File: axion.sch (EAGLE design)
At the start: 148 parts, among them IC1 3.3V, IC2 5V, Q2 12.288Mhz, U10 MIC2039, U11 WM8731, U2 Intel Edison, U4 FT232RLSSOP, U5 PCA9306D, U6 74HC4050, U7 TPA2005D1DGN, X1 MKDSN1,5/2-5,08, X2 ZX62R-AB-5P, X3 ST-005-G, X4 ZX62R-B-5P

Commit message: Change all resistors' package to R0603 (1608)
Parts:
- R1, R10, R11, R12, R13, R14, R15, R16, R17, R18, R19, R2, R20, R21, R22, R23, R24, R3, R30, R31, R32, R34, R36, R37, R4, R5, R6, R7, R8, R9: device resistor:R-US_M1206 -> resistor:R-US_R0603
- R25: device resistor:R-US_0309/V -> resistor:R-US_R0603
- R27, R35, R40, R41, R42, R43, R44: device resistor:R-US_R1206 -> resistor:R-US_R0603

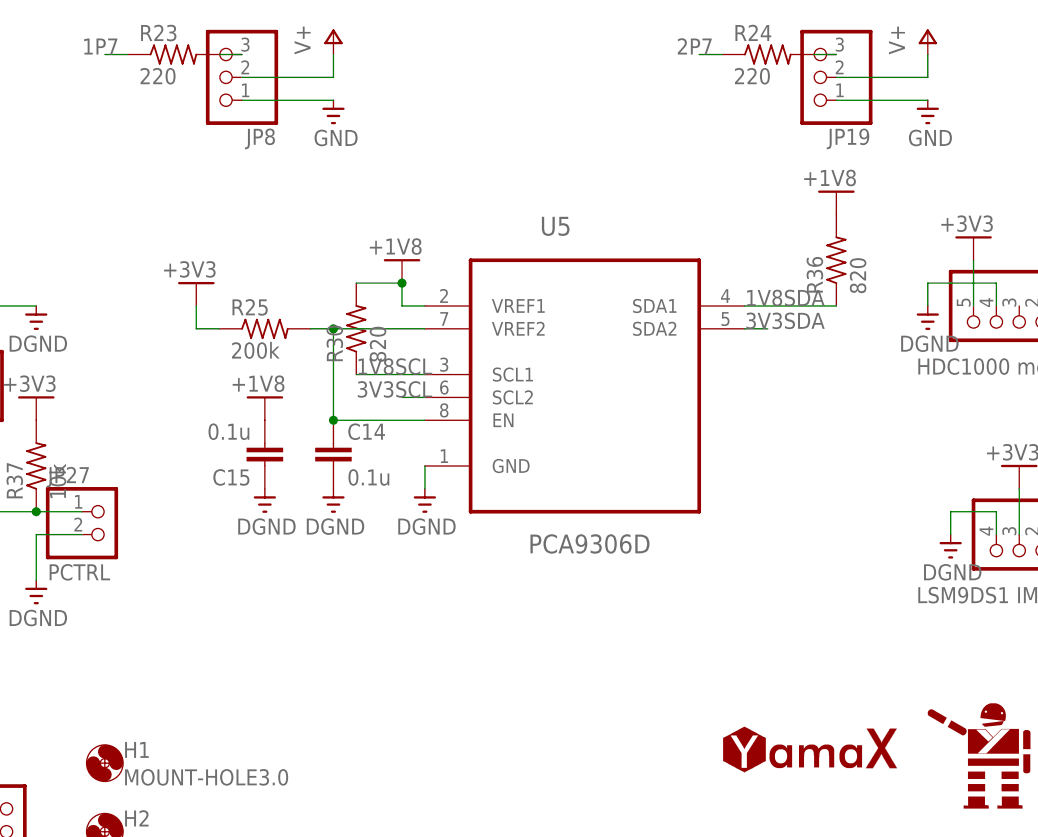
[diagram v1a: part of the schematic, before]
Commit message: Use BSS108 and 4.7k resistors for I2C level converter
Reference: https://www.intel.com/content/dam/support/us/en/documents/edison/sb/edison_arduino_hvm_8_26.pdf
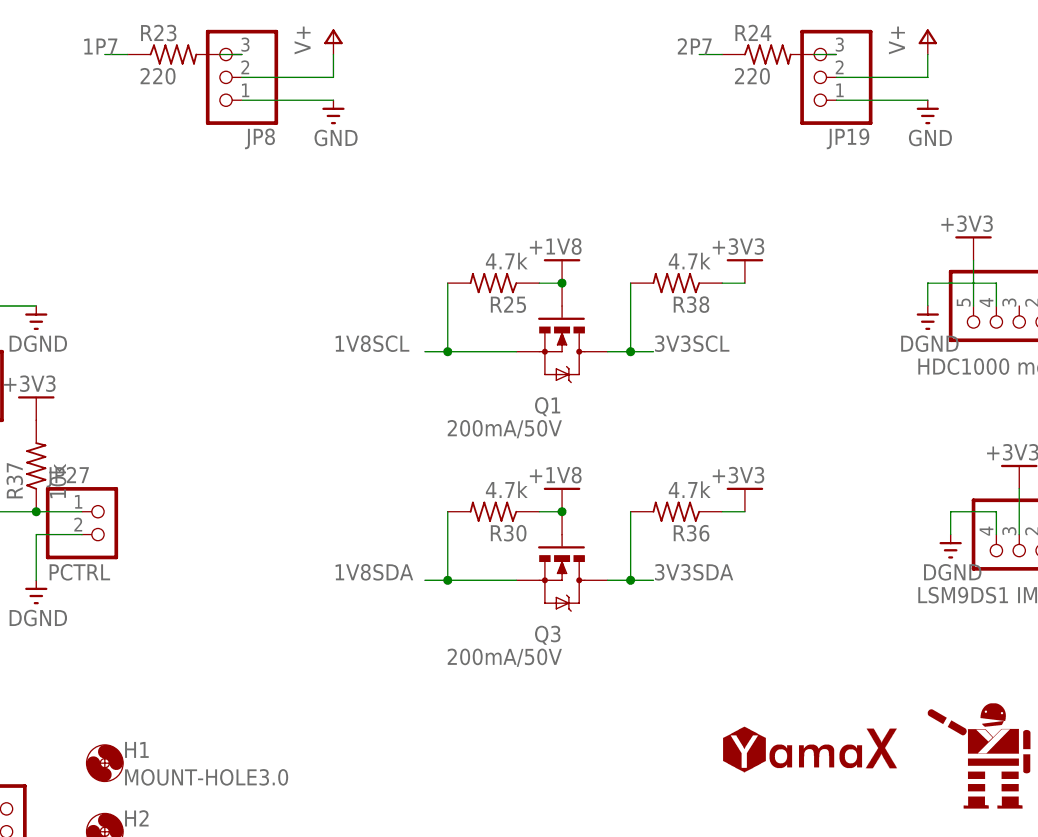
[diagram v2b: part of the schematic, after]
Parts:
- removed C14, C15: 0.1u, resistor:C-EUC1608
- removed U5: PCA9306D, NXP_By_element14_Batch_1:PCA9306D,118
- added Q1, Q3: 200mA/50V, SparkFun-DiscreteSemi:MOSFET-NCHANNELBSS138
- added R38: 4.7k, resistor:R-US_R0603
- R25: value 200k -> 4.7k
- R30, R36: value 820 -> 4.7k
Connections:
- removed net N$10: C14.1, R25.2, U5.EN, U5.VREF2
- net +1V8: now also Q1.G, Q3.G, R25.1, R30.1; no longer C15.2, R30.2, R36.2, U5.VREF1
- net +3V3: now also R36.1, R38.1; no longer R25.1
- net 1V8SCL: now also Q1.S, R25.2; no longer R30.1, U5.SCL1
- net 1V8SDA: now also Q3.S, R30.2; no longer R36.1, U5.SDA1
- net 3V3SCL: now also Q1.D, R38.2; no longer U5.SCL2
- net 3V3SDA: now also Q3.D, R36.2; no longer U5.SDA2
- net DGND: no longer C14.2, C15.1, U5.GND
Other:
- moved on the sheet: R25, R30, R36

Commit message: Fix many terrible mistakes
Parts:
- C24: device resistor:C-EUC0805 -> resistor:C-EUC1608
- JP26: value HDC1000 module -> HDC1000
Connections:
- removed net 1V8I2S_RTX: U8.A6
- removed net 3V3SCK: U11.SCLK
- removed net 5VCLK: U3.SCL
- net 1V8I2S_RXD: now also U8.A6
- net 3V3SCL: now also U11.SCLK, U3.SCL
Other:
- moved on the sheet: TP8
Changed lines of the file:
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@@
 <layers>
 <layer number="1" name="Top" color="4" fill="1" visible="yes" active="no"/>
-<layer number="2" name="Route2" color="1" fill="3" visible="no" active="no"/>
-<layer number="3" name="Route3" color="4" fill="3" visible="no" active="no"/>
-<layer number="4" name="Route4" color="1" fill="4" visible="no" active="no"/>
-<layer number="5" name="Route5" color="4" fill="4" visible="no" active="no"/>
-<layer number="6" name="Route6" color="1" fill="8" visible="no" active="no"/>
-<layer number="7" name="Route7" color="4" fill="8" visible="no" active="no"/>
-<layer number="8" name="Route8" color="1" fill="2" visible="no" active="no"/>
-<layer number="9" name="Route9" color="4" fill="2" visible="no" active="no"/>
-<layer number="10" name="Route10" color="1" fill="7" visible="no" active="no"/>
-<layer number="11" name="Route11" color="4" fill="7" visible="no" active="no"/>
-<layer number="12" name="Route12" color="1" fill="5" visible="no" active="no"/>
-<layer number="13" name="Route13" color="4" fill="5" visible="no" active="no"/>
-<layer number="14" name="Route14" color="1" fill="6" visible="no" active="no"/>
-<layer number="15" name="Route15" color="4" fill="6" visible="no" active="no"/>
+<layer number="2" name="Route2" color="1" fill="3" visible="yes" active="no"/>
+<layer number="3" name="Route3" color="4" fill="3" visible="yes" active="no"/>
+<layer number="4" name="Route4" color="1" fill="4" visible="yes" active="no"/>
+<layer number="5" name="Route5" color="4" fill="4" visible="yes" active="no"/>
+<layer number="6" name="Route6" color="1" fill="8" visible="yes" active="no"/>
+<layer number="7" name="Route7" color="4" fill="8" visible="yes" active="no"/>
+<layer number="8" name="Route8" color="1" fill="2" visible="yes" active="no"/>
+<layer number="9" name="Route9" color="4" fill="2" visible="yes" active="no"/>
+<layer number="10" name="Route10" color="1" fill="7" visible="yes" active="no"/>
+<layer number="11" name="Route11" color="4" fill="7" visible="yes" active="no"/>
+<layer number="12" name="Route12" color="1" fill="5" visible="yes" active="no"/>
+<layer number="13" name="Route13" color="4" fill="5" visible="yes" active="no"/>
+<layer number="14" name="Route14" color="1" fill="6" visible="yes" active="no"/>
+<layer number="15" name="Route15" color="4" fill="6" visible="yes" active="no"/>
 <layer number="16" name="Bottom" color="1" fill="1" visible="yes" active="no"/>
 <layer number="17" name="Pads" color="2" fill="1" visible="yes" active="no"/>
@@
 <part name="AGND9" library="supply0" deviceset="AGND" device=""/>
 <part name="AGND10" library="supply0" deviceset="AGND" device=""/>
-<part name="JP26" library="pinhead" deviceset="PINHD-1X5" device="" value="HDC1000 module"/>
+<part name="JP26" library="pinhead" deviceset="PINHD-1X5" device="" value="HDC1000"/>
 <part name="V31" library="supply0" deviceset="+3V3" device=""/>
 <part name="DGND27" library="supply0" deviceset="DGND" device=""/>
@@
 <part name="R40" library="resistor" deviceset="R-US_" device="R0603" value="330"/>
 <part name="C17" library="resistor" deviceset="CPOL-EU" device="E2-5" value="1u"/>
-<part name="C24" library="resistor" deviceset="C-EU" device="C0805" value="220p"/>
+<part name="C24" library="resistor" deviceset="C-EU" device="C1608" value="220p"/>
 <part name="AGND4" library="supply0" deviceset="AGND" device=""/>
 <part name="R41" library="resistor" deviceset="R-US_" device="R0603" value="5.6k"/>
@@
 <instance part="TP7" gate="G$1" x="35.56" y="-91.44" smashed="yes">
 <attribute name="TP_SIGNAL_NAME" x="36.83" y="-92.71" size="1.778" layer="97"/>
-<attribute name="NAME" x="34.29" y="-90.17" size="1.778" layer="95"/>
+<attribute name="NAME" x="36.83" y="-90.17" size="1.778" layer="95"/>
 </instance>
-<instance part="TP8" gate="G$1" x="35.56" y="-93.98" smashed="yes">
-<attribute name="TP_SIGNAL_NAME" x="36.83" y="-95.25" size="1.778" layer="97"/>
-<attribute name="NAME" x="34.29" y="-97.79" size="1.778" layer="95"/>
+<instance part="TP8" gate="G$1" x="38.1" y="-93.98" smashed="yes">
+<attribute name="TP_SIGNAL_NAME" x="39.37" y="-97.79" size="1.778" layer="97"/>
+<attribute name="NAME" x="39.37" y="-95.25" size="1.778" layer="95"/>
 </instance>
 <instance part="X4" gate="C" x="-119.38" y="20.32" rot="MR0"/>
@@
 <pinref part="U6" gate="G$1" pin="GND"/>
 <wire x1="58.42" y1="-38.1" x2="68.58" y2="-38.1" width="0.1524" layer="91"/>
+<junction x="68.58" y="-38.1"/>
 </segment>
 <segment>
@@
 <junction x="205.74" y="-73.66"/>
 </segment>
-</net>
-<net name="5VCLK" class="0">
+<segment>
+<pinref part="U11" gate="G$1" pin="SCLK"/>
+<wire x1="-91.44" y1="-104.14" x2="-93.98" y2="-104.14" width="0.1524" layer="91"/>
+<label x="-101.6" y="-104.14" size="1.778" layer="95"/>
+</segment>
 <segment>
 <pinref part="U3" gate="G$1" pin="SCL"/>
@@
 <label x="22.86" y="-96.52" size="1.778" layer="95"/>
 <pinref part="TP8" gate="G$1" pin="TP"/>
-<wire x1="20.32" y1="-96.52" x2="35.56" y2="-96.52" width="0.1524" layer="91"/>
+<wire x1="20.32" y1="-96.52" x2="38.1" y2="-96.52" width="0.1524" layer="91"/>
 </segment>
 <segment>
@@
 </segment>
 </net>
-<net name="3V3SCK" class="0">
-<segment>
-<pinref part="U11" gate="G$1" pin="SCLK"/>
-<wire x1="-91.44" y1="-104.14" x2="-93.98" y2="-104.14" width="0.1524" layer="91"/>
-<label x="-101.6" y="-104.14" size="1.778" layer="95"/>
-</segment>
-</net>
 <net name="N$70" class="0">
 <segment>
@@
 <label x="22.86" y="-76.2" size="1.778" layer="95"/>
 </segment>
-</net>
-<net name="1V8I2S_RTX" class="0">
 <segment>
 <pinref part="U8" gate="G$1" pin="A6"/>
